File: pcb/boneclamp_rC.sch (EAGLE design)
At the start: 133 parts, among them U1 OPA365AIDBVR, U10 AD5686, U11 LM2663, U12 MAX1735EUK25+T, U13 TLV70245DBVT, U14 REF5040MDREP, U15 AD8032ARZ-REEL7, U16 24C, U2 OPA365AIDBVR, U3 OPA365AIDBVR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

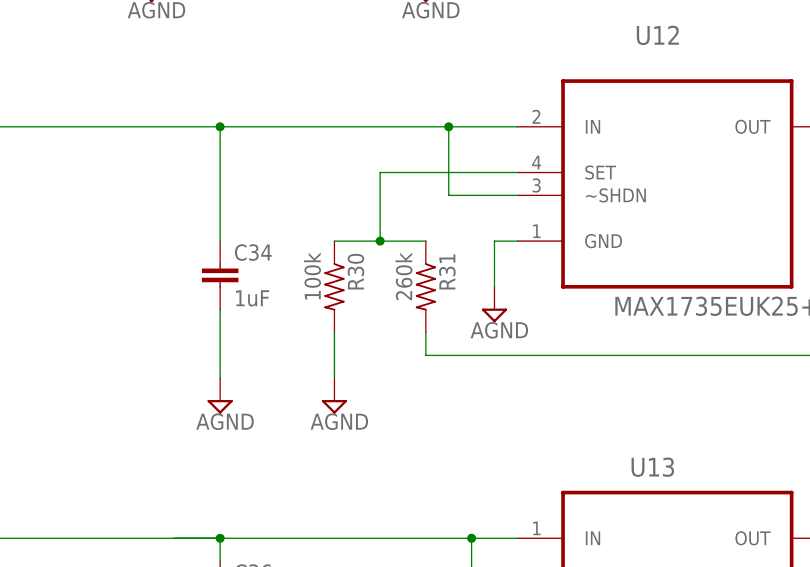
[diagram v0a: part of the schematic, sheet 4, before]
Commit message: Finished BOM.
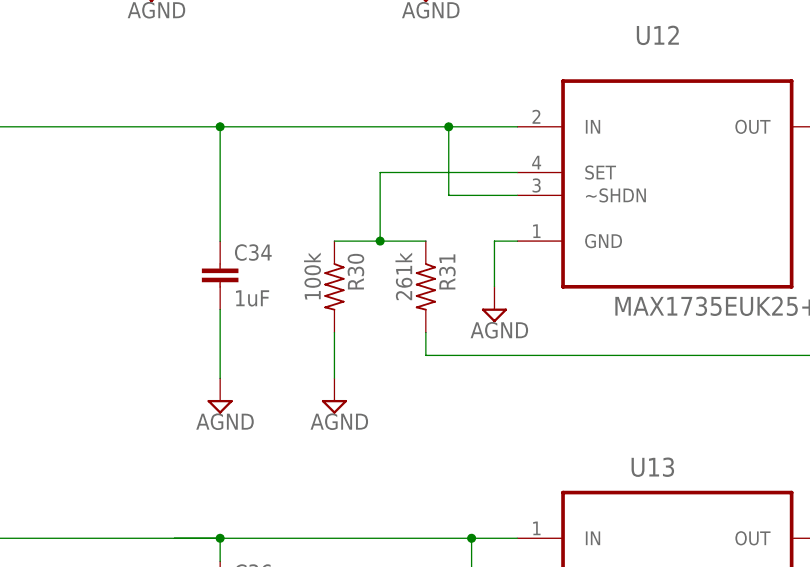
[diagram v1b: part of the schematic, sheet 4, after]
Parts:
- R31: value 260k -> 261k
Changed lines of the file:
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@@
 <part name="C35" library="rcl" deviceset="C-EU" device="C0603" value="1uF"/>
 <part name="R30" library="rcl" deviceset="R-US_" device="R0603" value="100k"/>
-<part name="R31" library="rcl" deviceset="R-US_" device="R0603" value="260k"/>
+<part name="R31" library="rcl" deviceset="R-US_" device="R0603" value="261k"/>
 <part name="U6" library="ti-extended" deviceset="OPA365AIDBVR" device=""/>
 <part name="R15" library="rcl" deviceset="R-US_" device="R0603" value="10k"/>

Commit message: Minor fix.
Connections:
- net ADC_A+: now also ADC_A+.TP
- net ADC_B+: now also ADC_B+.TP
- net ADC_C+: now also ADC_C+.TP
- net ADC_D+: now also ADC_D+.TP
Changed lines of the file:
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@@
 <junction x="-5.08" y="165.1"/>
 <label x="0" y="165.1" size="1.778" layer="95"/>
+<pinref part="ADC_B+" gate="G$1" pin="TP"/>
 </segment>
 </net>
@@
 <junction x="-5.08" y="226.06"/>
 <label x="0" y="226.06" size="1.778" layer="95"/>
+<pinref part="ADC_A+" gate="G$1" pin="TP"/>
 </segment>
 <segment>
@@
 <junction x="170.18" y="226.06"/>
 <label x="175.26" y="226.06" size="1.778" layer="95"/>
+<pinref part="ADC_C+" gate="G$1" pin="TP"/>
 </segment>
 </net>
@@
 <junction x="170.18" y="165.1"/>
 <label x="175.26" y="165.1" size="1.778" layer="95"/>
-</segment>
-</net>
+<pinref part="ADC_D+" gate="G$1" pin="TP"/>
+</segment>
+</net>

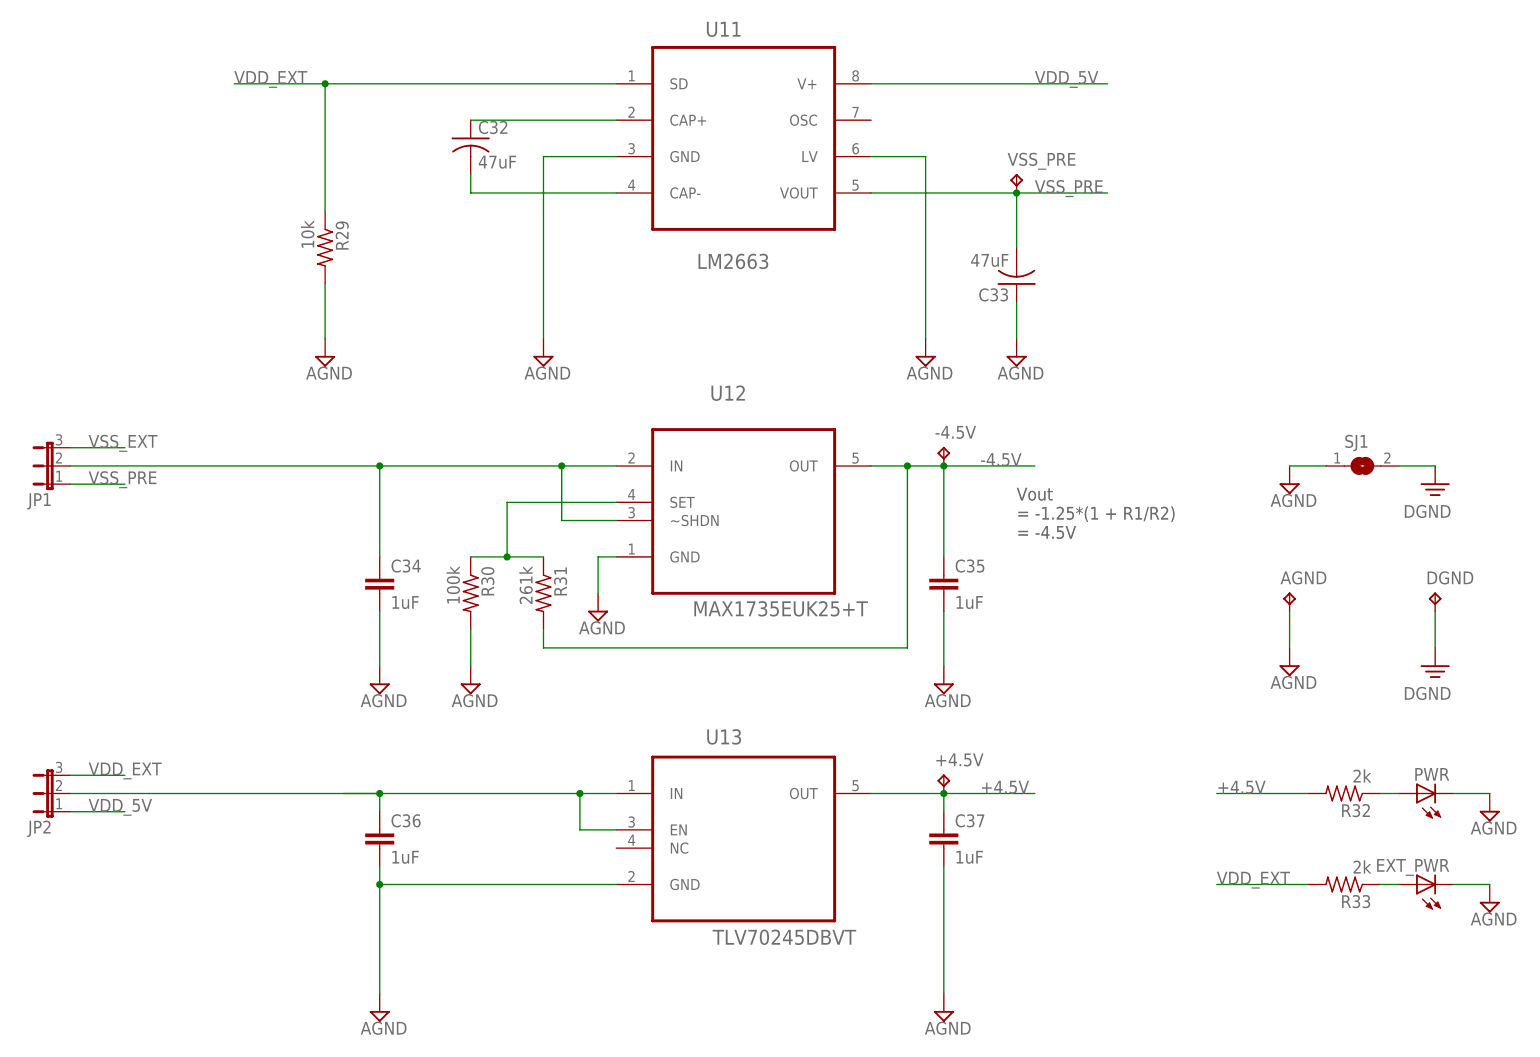
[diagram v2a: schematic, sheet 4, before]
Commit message: Finished switching voltage inverter layout.
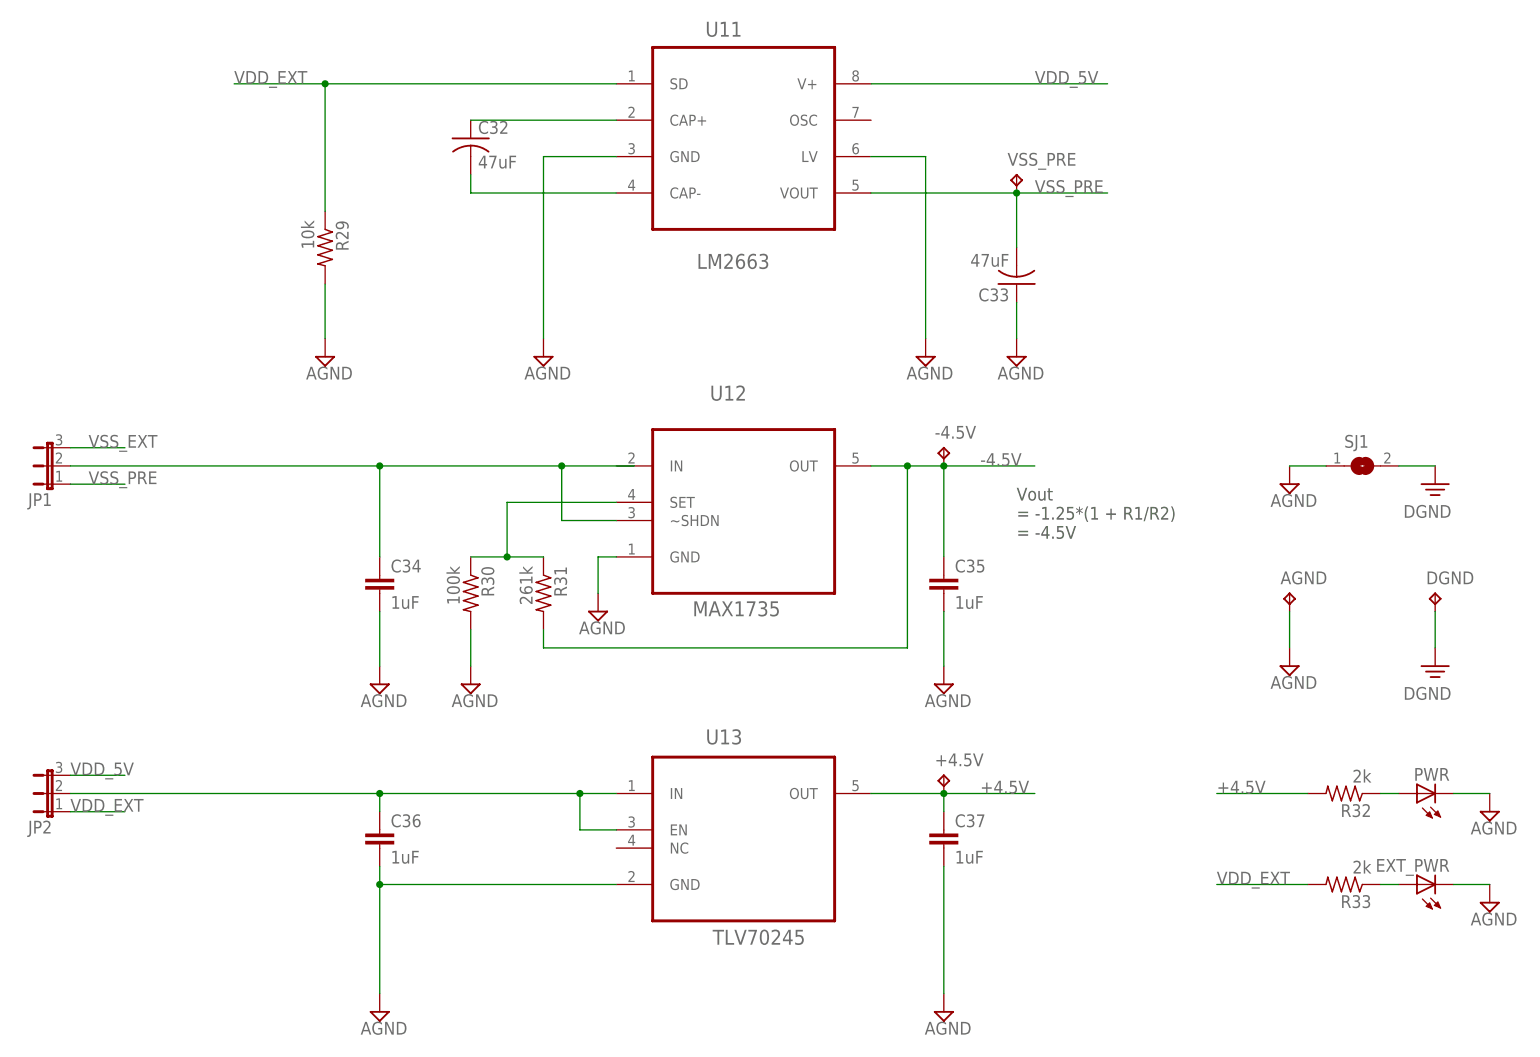
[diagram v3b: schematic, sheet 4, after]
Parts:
- U12: value MAX1735EUK25+T -> MAX1735
- U13: value TLV70245DBVT -> TLV70245
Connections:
- new net N$11: C36.1, JP2.2, U13.EN, U13.IN
- new net N$23: C34.1, JP1.2, U12.~SHDN
- net AGND: now also BB1.GND@2; no longer BB1.GND@5
- net DGND: no longer BB1.GND@6
- net VDD_5V: now also JP2.3; no longer C36.1, JP2.1, U13.EN, U13.IN
- net VDD_EXT: now also JP2.1
- net VSS_EXT: now also JP1.3
- net VSS_PRE: no longer C34.1, JP1.2, JP2.2, U12.IN, U12.~SHDN
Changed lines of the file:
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@@
 <part name="I2C2_SCLK" library="testpad" deviceset="TP" device="B1,27"/>
 <part name="VDRIVE" library="testpad" deviceset="TP" device="B1,27"/>
-<part name="U13" library="ti-extended" deviceset="TLV70025DDCR" device="" value="TLV70245DBVT"/>
+<part name="U13" library="ti-extended" deviceset="TLV70025DDCR" device="" value="TLV70245"/>
 <part name="C36" library="rcl" deviceset="C-EU" device="C0603" value="1uF"/>
 <part name="C37" library="rcl" deviceset="C-EU" device="C0603" value="1uF"/>
@@
 <part name="C43" library="rcl" deviceset="C-EU" device="C0603" value="0.1uF"/>
 <part name="A_I/O" library="adafruit" deviceset="PINHD-2X5" device="/90"/>
-<part name="U12" library="Maxim_By_element14_Batch_1" deviceset="MAX1735EUK25+T" device=""/>
+<part name="U12" library="Maxim_By_element14_Batch_1" deviceset="MAX1735EUK25+T" device="" value="MAX1735"/>
 <part name="C34" library="rcl" deviceset="C-EU" device="C0603" value="1uF"/>
 <part name="SUPPLY3" library="supply2" deviceset="AGND" device=""/>
@@
 <instance part="BB1" gate="G$1" x="-35.56" y="48.26"/>
 <instance part="DGND2" gate="PE" x="2.54" y="-20.32"/>
-<instance part="SUPPLY8" gate="G$1" x="10.16" y="-20.32"/>
+<instance part="SUPPLY8" gate="G$1" x="17.78" y="33.02"/>
 <instance part="A_I/O" gate="G$1" x="53.34" y="30.48"/>
 <instance part="PWR_EXT" gate="A" x="53.34" y="7.62"/>
@@
 <net name="DGND" class="0">
 <segment>
-<wire x1="2.54" y1="-12.7" x2="2.54" y2="-17.78" width="0.1524" layer="91"/>
-<pinref part="DGND2" gate="PE" pin="PE"/>
-</segment>
-<segment>
-<pinref part="BB1" gate="G$1" pin="GND@6"/>
-<wire x1="-7.62" y1="-12.7" x2="2.54" y2="-12.7" width="0.1524" layer="91"/>
-</segment>
-<segment>
 <pinref part="RESET" gate="G$1" pin="S"/>
 <pinref part="RESET" gate="G$1" pin="S1"/>
@@
 <net name="AGND" class="0">
 <segment>
-<pinref part="BB1" gate="G$1" pin="GND@5"/>
-<wire x1="-7.62" y1="-10.16" x2="10.16" y2="-10.16" width="0.1524" layer="91"/>
-<wire x1="10.16" y1="-10.16" x2="10.16" y2="-17.78" width="0.1524" layer="91"/>
+<wire x1="17.78" y1="43.18" x2="17.78" y2="35.56" width="0.1524" layer="91"/>
 <pinref part="SUPPLY8" gate="G$1" pin="AGND"/>
+<pinref part="BB1" gate="G$1" pin="GND@2"/>
+<wire x1="-7.62" y1="43.18" x2="17.78" y2="43.18" width="0.1524" layer="91"/>
 </segment>
 <segment>
@@
 <pinref part="PWR_EXT" gate="A" pin="1"/>
 <label x="35.56" y="10.16" size="1.778" layer="95"/>
-</segment>
-</net>
-<net name="VSS_EXT" class="0">
-<segment>
-<wire x1="35.56" y1="5.08" x2="50.8" y2="5.08" width="0.1524" layer="91"/>
-<pinref part="PWR_EXT" gate="A" pin="3"/>
-<label x="35.56" y="5.08" size="1.778" layer="95"/>
 </segment>
 </net>
@@
 <junction x="76.2" y="5.08"/>
 <label x="66.04" y="5.08" size="1.778" layer="95"/>
+</segment>
+</net>
+<net name="VSS_EXT" class="0">
+<segment>
+<pinref part="PWR_EXT" gate="A" pin="3"/>
+<wire x1="35.56" y1="5.08" x2="50.8" y2="5.08" width="0.1524" layer="91"/>
+<label x="35.56" y="5.08" size="1.778" layer="95"/>
 </segment>
 </net>
@@
 <net name="VDD_5V" class="0">
 <segment>
-<pinref part="U13" gate="A" pin="IN"/>
-<wire x1="-15.24" y1="-55.88" x2="-20.32" y2="-55.88" width="0.1524" layer="91"/>
-<pinref part="C36" gate="G$1" pin="1"/>
-<wire x1="-20.32" y1="-55.88" x2="-48.26" y2="-55.88" width="0.1524" layer="91"/>
-<wire x1="-48.26" y1="-55.88" x2="-53.34" y2="-55.88" width="0.1524" layer="91"/>
-<wire x1="-48.26" y1="-58.42" x2="-48.26" y2="-55.88" width="0.1524" layer="91"/>
-<junction x="-48.26" y="-55.88"/>
-<wire x1="-20.32" y1="-55.88" x2="-20.32" y2="-60.96" width="0.1524" layer="91"/>
-<junction x="-20.32" y="-55.88"/>
-<pinref part="U13" gate="A" pin="EN"/>
-<wire x1="-20.32" y1="-60.96" x2="-15.24" y2="-60.96" width="0.1524" layer="91"/>
-</segment>
-<segment>
 <pinref part="U11" gate="G$1" pin="V+"/>
 <wire x1="53.34" y1="43.18" x2="20.32" y2="43.18" width="0.1524" layer="91"/>
@@
 </segment>
 <segment>
-<pinref part="JP2" gate="1" pin="1"/>
-<wire x1="-91.44" y1="-58.42" x2="-83.82" y2="-58.42" width="0.1524" layer="91"/>
-<label x="-88.9" y="-58.42" size="1.778" layer="95"/>
+<pinref part="JP2" gate="1" pin="3"/>
+<wire x1="-91.44" y1="-53.34" x2="-83.82" y2="-53.34" width="0.1524" layer="91"/>
+<label x="-91.44" y="-53.34" size="1.778" layer="95"/>
 </segment>
 </net>
@@
 </segment>
 <segment>
-<pinref part="C34" gate="G$1" pin="1"/>
-<wire x1="-15.24" y1="-10.16" x2="-22.86" y2="-10.16" width="0.1524" layer="91"/>
-<wire x1="-22.86" y1="-10.16" x2="-48.26" y2="-10.16" width="0.1524" layer="91"/>
-<wire x1="-48.26" y1="-22.86" x2="-48.26" y2="-10.16" width="0.1524" layer="91"/>
-<pinref part="U12" gate="A" pin="IN"/>
-<pinref part="U12" gate="A" pin="~SHDN"/>
-<wire x1="-15.24" y1="-17.78" x2="-22.86" y2="-17.78" width="0.1524" layer="91"/>
-<wire x1="-22.86" y1="-17.78" x2="-22.86" y2="-10.16" width="0.1524" layer="91"/>
-<junction x="-22.86" y="-10.16"/>
-<pinref part="JP1" gate="1" pin="2"/>
-<wire x1="-91.44" y1="-10.16" x2="-48.26" y2="-10.16" width="0.1524" layer="91"/>
-<junction x="-48.26" y="-10.16"/>
-</segment>
-<segment>
 <pinref part="JP1" gate="1" pin="1"/>
 <wire x1="-91.44" y1="-12.7" x2="-83.82" y2="-12.7" width="0.1524" layer="91"/>
 <label x="-88.9" y="-12.7" size="1.778" layer="95"/>
-</segment>
-<segment>
-<pinref part="JP2" gate="1" pin="2"/>
-<wire x1="-91.44" y1="-55.88" x2="-48.26" y2="-55.88" width="0.1524" layer="91"/>
 </segment>
 </net>
@@
 </segment>
 </net>
-<net name="VSS_EXT" class="0">
-<segment>
-<wire x1="-91.44" y1="-7.62" x2="-83.82" y2="-7.62" width="0.1524" layer="91"/>
-<label x="-88.9" y="-7.62" size="1.778" layer="95"/>
-</segment>
-</net>
 <net name="VDD_EXT" class="0">
-<segment>
-<wire x1="-91.44" y1="-53.34" x2="-83.82" y2="-53.34" width="0.1524" layer="91"/>
-<label x="-88.9" y="-53.34" size="1.778" layer="95"/>
-</segment>
 <segment>
 <pinref part="U11" gate="G$1" pin="SD"/>
@@
 <wire x1="81.28" y1="-68.58" x2="68.58" y2="-68.58" width="0.1524" layer="91"/>
 </segment>
+<segment>
+<pinref part="JP2" gate="1" pin="1"/>
+<wire x1="-91.44" y1="-58.42" x2="-83.82" y2="-58.42" width="0.1524" layer="91"/>
+<label x="-91.44" y="-58.42" size="1.778" layer="95"/>
+</segment>
 </net>
 <net name="N$20" class="0">
@@
 </segment>
 </net>
+<net name="N$11" class="0">
+<segment>
+<pinref part="U13" gate="A" pin="EN"/>
+<wire x1="-15.24" y1="-60.96" x2="-20.32" y2="-60.96" width="0.1524" layer="91"/>
+<wire x1="-20.32" y1="-60.96" x2="-20.32" y2="-55.88" width="0.1524" layer="91"/>
+<pinref part="U13" gate="A" pin="IN"/>
+<pinref part="C36" gate="G$1" pin="1"/>
+<wire x1="-15.24" y1="-55.88" x2="-20.32" y2="-55.88" width="0.1524" layer="91"/>
+<wire x1="-20.32" y1="-55.88" x2="-48.26" y2="-55.88" width="0.1524" layer="91"/>
+<wire x1="-48.26" y1="-55.88" x2="-48.26" y2="-58.42" width="0.1524" layer="91"/>
+<pinref part="JP2" gate="1" pin="2"/>
+<wire x1="-48.26" y1="-55.88" x2="-91.44" y2="-55.88" width="0.1524" layer="91"/>
+<junction x="-48.26" y="-55.88"/>
+<junction x="-20.32" y="-55.88"/>
+</segment>
+</net>
+<net name="N$23" class="0">
+<segment>
+<pinref part="U12" gate="A" pin="~SHDN"/>
+<wire x1="-15.24" y1="-17.78" x2="-22.86" y2="-17.78" width="0.1524" layer="91"/>
+<wire x1="-22.86" y1="-17.78" x2="-22.86" y2="-10.16" width="0.1524" layer="91"/>
+<pinref part="C34" gate="G$1" pin="1"/>
+<wire x1="-12.7" y1="-10.16" x2="-22.86" y2="-10.16" width="0.1524" layer="91"/>
+<wire x1="-22.86" y1="-10.16" x2="-48.26" y2="-10.16" width="0.1524" layer="91"/>
+<wire x1="-48.26" y1="-10.16" x2="-48.26" y2="-22.86" width="0.1524" layer="91"/>
+<pinref part="JP1" gate="1" pin="2"/>
+<wire x1="-48.26" y1="-10.16" x2="-91.44" y2="-10.16" width="0.1524" layer="91"/>
+<junction x="-48.26" y="-10.16"/>
+<junction x="-22.86" y="-10.16"/>
+</segment>
+</net>
+<net name="VSS_EXT" class="0">
+<segment>
+<pinref part="JP1" gate="1" pin="3"/>
+<wire x1="-83.82" y1="-7.62" x2="-91.44" y2="-7.62" width="0.1524" layer="91"/>
+<label x="-88.9" y="-7.62" size="1.778" layer="95"/>
+</segment>
+</net>

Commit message: Routed VDRIVE out from bbehind switching supply using power plane. Following regulation +/-4.5v will dive into power plane and occupy it with VDRIVE. SPI signals should originate from p8 if at all possible.
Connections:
- net -4.5V: now also -4.5V.TP
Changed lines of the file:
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@@
 <pinref part="U12" gate="A" pin="OUT"/>
 <wire x1="20.32" y1="-10.16" x2="25.4" y2="-10.16" width="0.1524" layer="91"/>
-<pinref part="C35" gate="G$1" pin="1"/>
 <wire x1="25.4" y1="-10.16" x2="30.48" y2="-10.16" width="0.1524" layer="91"/>
+<pinref part="R31" gate="G$1" pin="2"/>
 <wire x1="30.48" y1="-10.16" x2="43.18" y2="-10.16" width="0.1524" layer="91"/>
-<wire x1="30.48" y1="-22.86" x2="30.48" y2="-10.16" width="0.1524" layer="91"/>
-<junction x="30.48" y="-10.16"/>
-<pinref part="R31" gate="G$1" pin="2"/>
 <wire x1="-25.4" y1="-33.02" x2="-25.4" y2="-35.56" width="0.1524" layer="91"/>
 <wire x1="-25.4" y1="-35.56" x2="25.4" y2="-35.56" width="0.1524" layer="91"/>
@@
 <junction x="25.4" y="-10.16"/>
 <label x="35.56" y="-10.16" size="1.778" layer="95"/>
+<pinref part="C35" gate="G$1" pin="1"/>
+<wire x1="30.48" y1="-22.86" x2="30.48" y2="-10.16" width="0.1524" layer="91"/>
+<pinref part="-4.5V" gate="G$1" pin="TP"/>
+<junction x="30.48" y="-10.16"/>
 </segment>
 </net>
